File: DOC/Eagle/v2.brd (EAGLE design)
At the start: 100 x 80 mm, 18 parts, among them M1 RF-LORA-868-SO, X1 SMA-142-0701-871/876

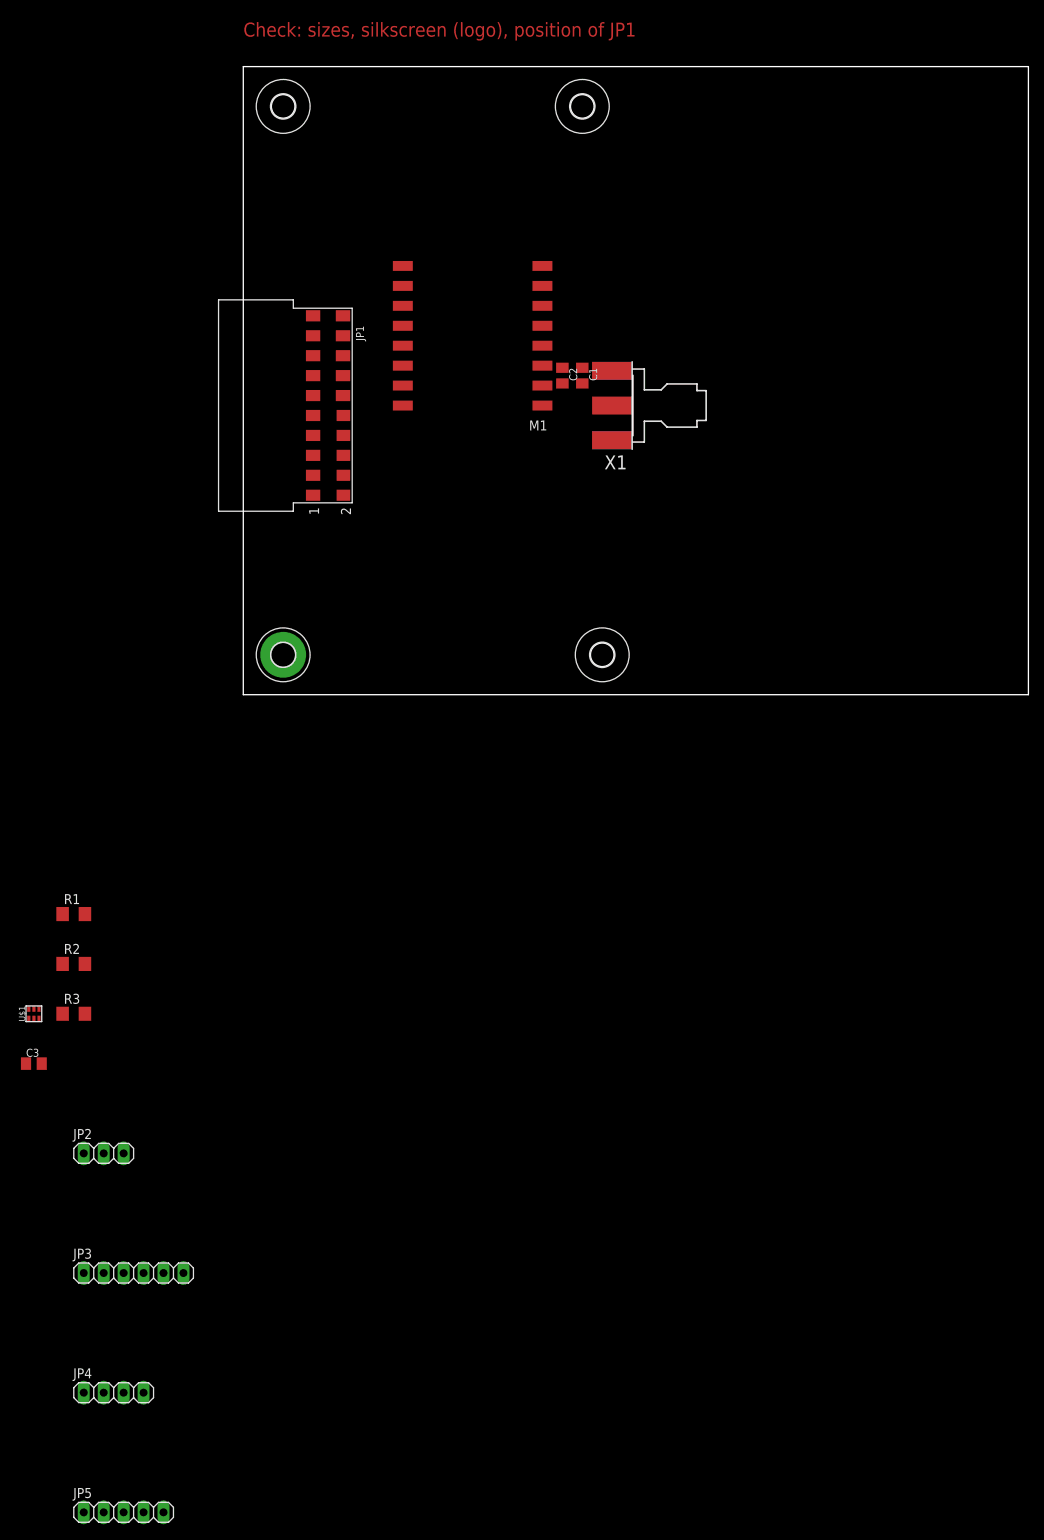
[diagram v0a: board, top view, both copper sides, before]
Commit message: Updated hardware design
Finished schematic (final checks needed!)
Included pdf of the schematic
First version of the board (no silkscreen yet)
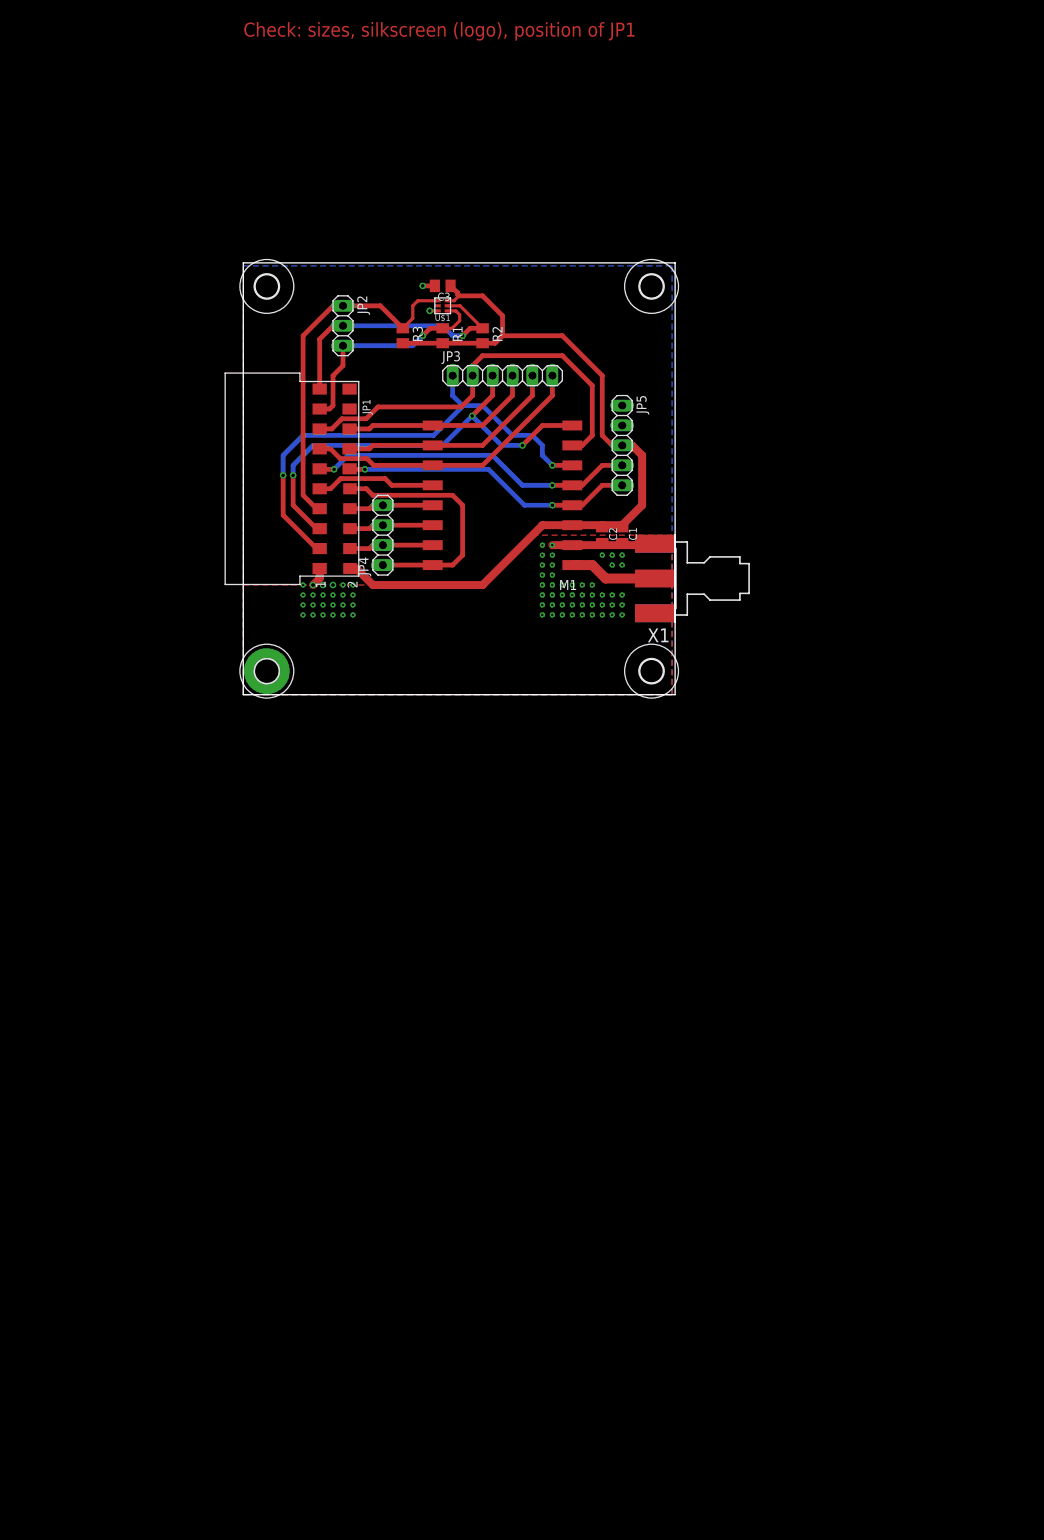
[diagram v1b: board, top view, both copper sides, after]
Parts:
- R1, R2, R3: device rcl:R1206 -> rcl:M0805
- moved JP5 150.0 mm to (48.3, 31.8), turned to 270 degrees
- moved JP3 123.6 mm to (33.0, 40.6)
- moved JP4 114.5 mm to (17.8, 20.3), turned to 90 degrees
- moved C3 111.9 mm to (25.4, 52.1), turned to 180 degrees
- moved JP2 109.7 mm to (12.7, 47.0), turned to 270 degrees
- moved U$1 104.1 mm to (25.4, 49.5), turned to 90 degrees
- moved R3 96.0 mm to (20.3, 45.7), turned to 270 degrees
- moved R2 95.5 mm to (30.5, 45.7), turned to 270 degrees
- moved R1 87.4 mm to (25.4, 45.7), turned to 270 degrees
- moved H3 24.6 mm to (52.0, 52.0)
- moved H2 23.0 mm to (3.00, 52.0)
- moved X1 22.7 mm to (55.0, 14.8)
- moved C1 20.9 mm to (48.3, 20.3)
- moved C2 20.9 mm to (45.7, 20.3)
- moved M1 20.7 mm to (33.0, 25.4)
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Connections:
- net SDI: now also JP4.2; no longer JP4.3
- net SDO: now also JP4.3; no longer JP4.2
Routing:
- net VCC: track 0.00 -> 103.5 mm
- net DIO0: track 0.00 -> 61.8 mm, vias 0 -> 2
- net DIO2: track 0.00 -> 56.7 mm, vias 0 -> 3
- net DIO1: track 0.00 -> 51.8 mm
- net LIGHT_SENSE_INT: track 0.00 -> 45.4 mm
- net TX_SWITCH: track 0.00 -> 41.9 mm, vias 0 -> 2
- net RX_SWITCH: track 0.00 -> 37.7 mm, vias 0 -> 2
- net DIO5: track 0.00 -> 36.7 mm
- net LIGHT_SENSE_SDA: track 0.00 -> 34.3 mm, vias 0 -> 1
- net !CS: track 0.00 -> 32.3 mm
- net LIGHT_SENSE_SCL: track 0.00 -> 28.7 mm, vias 0 -> 1
- net DIO4: track 0.00 -> 28.6 mm
- net DIO3: track 0.00 -> 25.1 mm
- net GND: track 0.00 -> 18.7 mm, vias 0 -> 42
- net RST: track 0.00 -> 15.3 mm
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- added copper zone on layer 1, net GND
- added copper zone on layer 16, net GND
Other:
- board size 100 x 80 mm -> 55 x 55 mm

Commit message: Updated board design
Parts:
- H1, H2, H3: value MOUNT-HOLE3.0 -> MOUNT-PAD-ROUND3.0; device holes:3,0 -> holes:3,0-PAD
- moved H1 49.0 mm to (52.0, 52.0)
- moved H3 49.0 mm to (52.0, 3.00)
- renumbered U$1 to IC1
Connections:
- net GND: now also H1.B3,0, H2.B3,0, H3.B3,0
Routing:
- net GND: track 18.7 -> 14.6 mm, vias 42 -> 34
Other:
- board text added: "!CS"
- board text added: "0"
- board text added: "1"
- board text added: "2"
- board text added: "3"
- board text added: "4"
- board text added: "5"
- board text added: "DIO"
- board text added: "DRAMCO research group"
- board text added: "Design by:"
- board text added: "EFM32 Wonder Gecko"
- board text added: "EFM32 Wonder Gecko LoRa Extension Board"
- board text added: "GND"
- board text added: "Geoffrey Ottoy & Gilles Callebaut"
- board text added: "INT"
- board text added: "KU Leuven - Technology Campus Ghent"
- board text added: "Light Sense"
- board text added: "LoRa Extension Board (v2.0)"
- board text added: "RF-LORA-868"
- board text added: "RX"
- board text added: "SCK"
- board text added: "SCL"
- board text added: "SDA"
- board text added: "SDI"
- board text added: "SDO"
- board text added: "SPI"
- board text added: "Switch"
- board text added: "TX"
- board text added: "VCC"
- board text removed: "Check: sizes!, silkscreen (logo), position of JP1"

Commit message: Final touches to board design, Gerber files
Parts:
- H1, H2, H3, H4: value MOUNT-PAD-ROUND3.0 -> MOUNT-HOLE3.0; device holes:3,0-PAD -> holes:3,0
- moved H1 69.3 mm to (3.00, 3.00)
- moved H2 69.3 mm to (52.0, 3.00)
- moved H3 49.0 mm to (52.0, 52.0)
- moved H4 49.0 mm to (3.00, 52.0)
- moved C3 3.31 mm to (28.7, 51.8), turned to 90 degrees
- moved R1 2.29 mm to (27.7, 45.7)
- moved R2 0.76 mm to (29.7, 45.7)
- moved JP4 0.52 mm to (17.9, 19.8)
- moved M1 0.51 mm to (33.0, 24.9)
- moved X1 0.25 mm to (54.7, 14.8)
- moved C2 0.18 mm to (45.8, 20.4)
- moved C1 0.13 mm to (48.3, 20.4)
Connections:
- net GND: no longer H1.B3,0, H2.B3,0, H3.B3,0, H4.B3,0
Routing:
- net GND: track 14.6 -> 5.44 mm, vias 34 -> 33
- net LIGHT_SENSE_SCL: track 28.7 -> 30.9 mm
- net VCC: track 103.5 -> 105.3 mm
- net LIGHT_SENSE_SDA: track 34.3 -> 33.6 mm
- net ANT: track 11.4 -> 10.8 mm
- net !CS: track 32.3 -> 31.6 mm
- net DIO0: track 61.8 -> 62.4 mm
- added copper zone on layer 1, net TEST
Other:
- board text added: "Designed by: Geoffrey Ottoy, Gilles Callebaut, Guus Leenders"
- board text removed: "Design by:"
- board text removed: "Geoffrey Ottoy & Gilles Callebaut"
